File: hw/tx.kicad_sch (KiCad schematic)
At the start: 40 parts, among them T301 BN-43-202_DualPri_CTSec, U301 ICE40UP5K-SG48ITR, Y301 40MHz

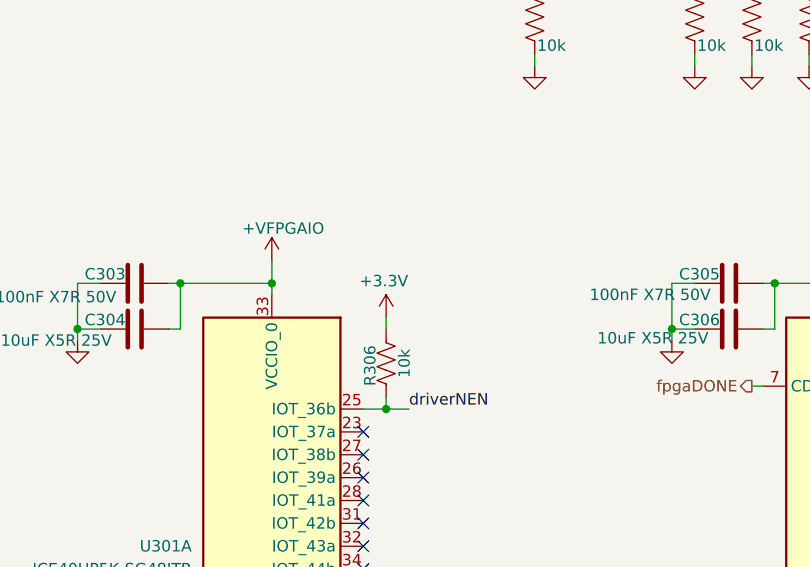
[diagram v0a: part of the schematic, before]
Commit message: Use VFPGAIO for pullup for driverNEN. Fix some layout issues with more equal routing lengths in critical tx phase paths.
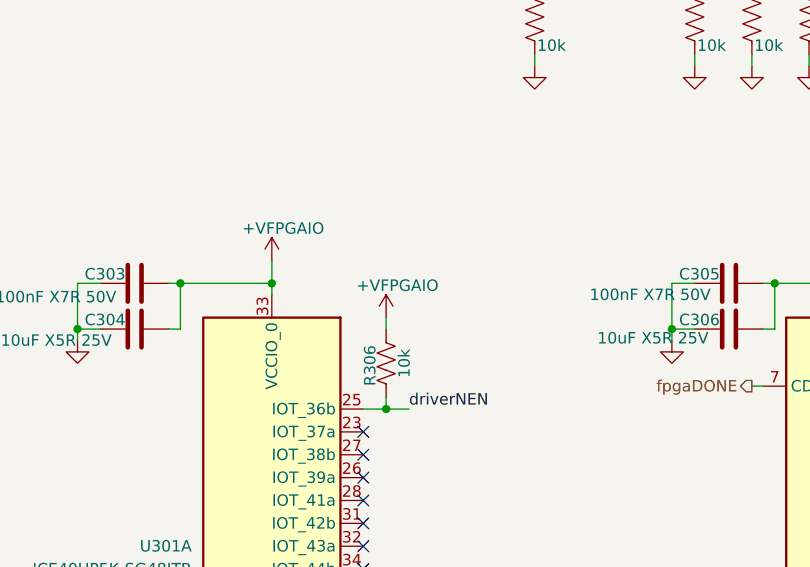
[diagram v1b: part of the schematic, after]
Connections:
- net +3.3V: no longer R306.2
- net +VFPGAIO: now also R306.2
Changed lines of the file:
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@@
-	)
-	(symbol
-		(lib_id "power:+3.3V")
-		(at 66.04 139.7 0)
-		(unit 1)
-		(exclude_from_sim no)
-		(in_bom yes)
-		(on_board yes)
-		(dnp no)
-		(property "Reference" "#PWR0305"
-			(at 66.04 143.51 0)
-			(effects
-				(font
-					(size 1.27 1.27)
-				)
-				(hide yes)
-			)
-		)
-		(property "Value" "+3.3V"
-			(at 65.786 135.636 0)
-			(effects
-				(font
-					(size 1.27 1.27)
-				)
-			)
-		)
-		(property "Footprint" ""
-			(at 66.04 139.7 0)
-			(effects
-				(font
-					(size 1.27 1.27)
-				)
-				(hide yes)
-			)
-		)
-		(property "Datasheet" ""
-			(at 66.04 139.7 0)
-			(effects
-				(font
-					(size 1.27 1.27)
-				)
-				(hide yes)
-			)
-		)
-		(property "Description" "Power symbol creates a global label with name \"+3.3V\""
-			(at 66.04 139.7 0)
-			(effects
-				(font
-					(size 1.27 1.27)
-				)
-				(hide yes)
-			)
-		)
-		(pin "1"
-		)
-		(instances
-			(project "WSPR-ease"
-				(path "/31075357-d7d2-474d-bd47-511c83e129b3/23b3e7ef-2325-4c00-b23e-f86801b0fb79"
-					(reference "#PWR0305")
-					(unit 1)
-				)
-			)
-		)
 	)
 	(symbol
@@
 					(unit 1)
 				)
+			)
+		)
+	)
+	(symbol
+		(lib_id "power:+3.3V")
+		(at 66.04 139.7 0)
+		(unit 1)
+		(exclude_from_sim no)
+		(in_bom yes)
+		(on_board yes)
+		(dnp no)
+		(property "Reference" "#PWR0305"
+			(at 66.04 143.51 0)
+			(effects
+				(font
+					(size 1.27 1.27)
+				)
+				(hide yes)
+			)
+		)
+		(property "Value" "+VFPGAIO"
+			(at 62.738 136.144 0)
+			(effects
+				(font
+					(size 1.27 1.27)
+				)
+				(justify left)
+			)
+		)
+		(property "Footprint" ""
+			(at 66.04 139.7 0)
+			(effects
+				(font
+					(size 1.27 1.27)
+				)
+				(hide yes)
+			)
+		)
+		(property "Datasheet" ""
+			(at 66.04 139.7 0)
+			(effects
+				(font
+					(size 1.27 1.27)
+				)
+				(hide yes)
+			)
+		)
+		(property "Description" "Power symbol creates a global label with name \"+VFPGAIO\""
+			(at 66.04 139.7 0)
+			(effects
+				(font
+					(size 1.27 1.27)
+				)
+				(hide yes)
+			)
+		)
+		(pin "1"
+		)
+		(instances
+			(project "WSPR-ease"
+				(path "/31075357-d7d2-474d-bd47-511c83e129b3/23b3e7ef-2325-4c00-b23e-f86801b0fb79"
+					(reference "#PWR0305")
+					(unit 1)
+				)

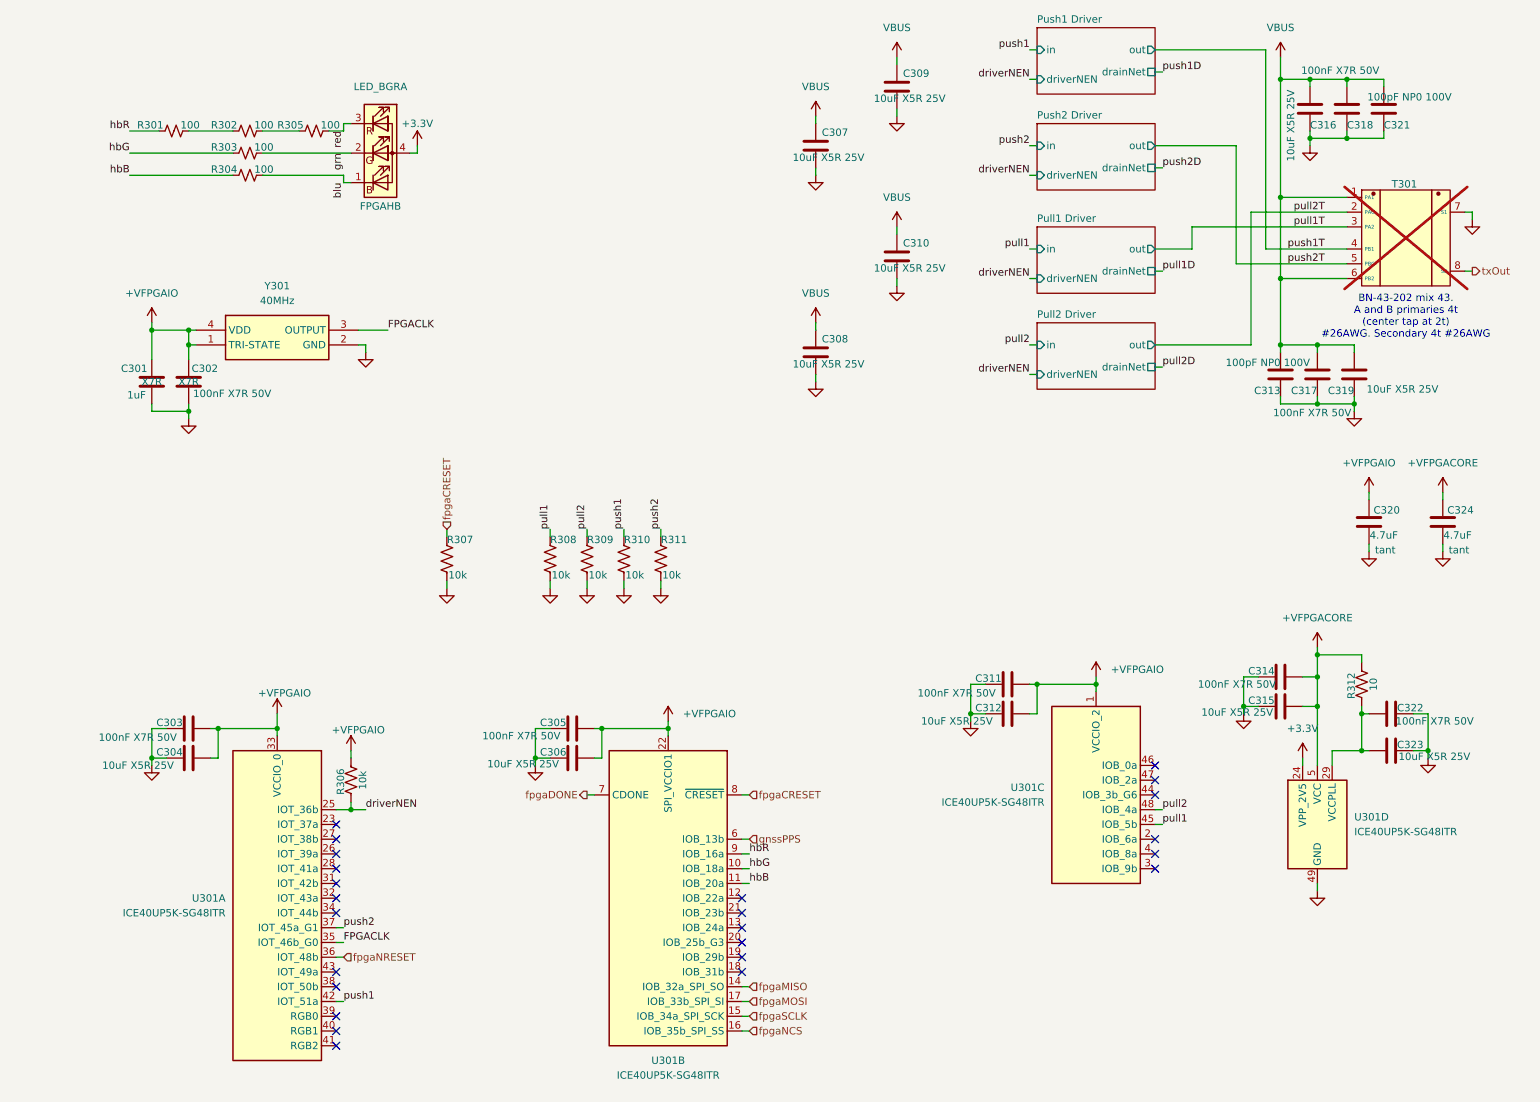
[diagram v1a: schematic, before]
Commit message: I think this is now using the SB_MAC16 properly for each instance. The AI based configs were all screwed up. I listed teh name from the iCE40 Tech Lib doc for each flavor used in a comment to help if changes are needed later. Also silkscreen labels for the four FPGA output pins for probing. I also fixed some stuff in the SB_IO sim cells_sim.v that seemed wrong but now it matches the PDF block diagram AFACT.
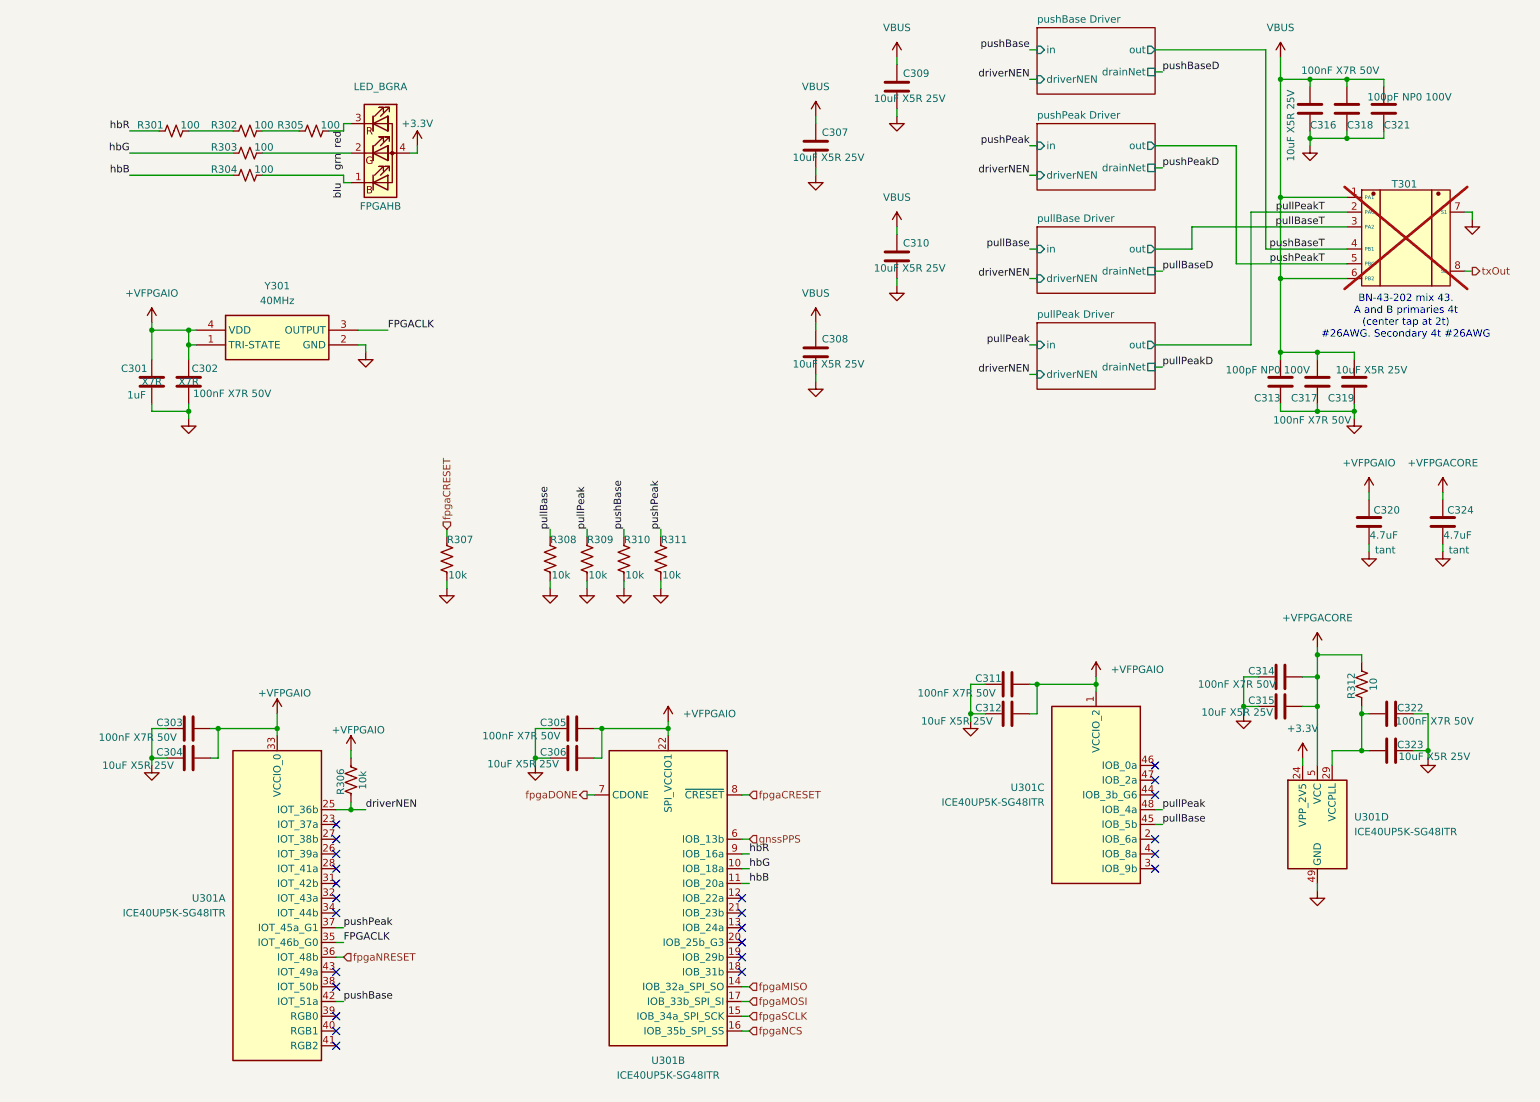
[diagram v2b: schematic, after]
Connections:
- net pull1 renamed pullBase
- net pull1T renamed pullBaseT
- net pull2 renamed pullPeak
- net pull2T renamed pullPeakT
- net push1 renamed pushBase
- net push1T renamed pushBaseT
- net push2 renamed pushPeak
- net push2T renamed pushPeakT
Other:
- sheet Pull1 Driver renamed pullBase Driver
- sheet Pull2 Driver renamed pullPeak Driver
- sheet Push1 Driver renamed pushBase Driver
- sheet Push2 Driver renamed pushPeak Driver
- moved on the sheet: C313, C317, C319

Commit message: Fucking USB 16-pin footprint! Also, completely redid the layout and wiring of the transmitter using a MOSFET gate and R+diode gate drive, simplify BOM, enhance LPFs for square wave output >= 10MHz.
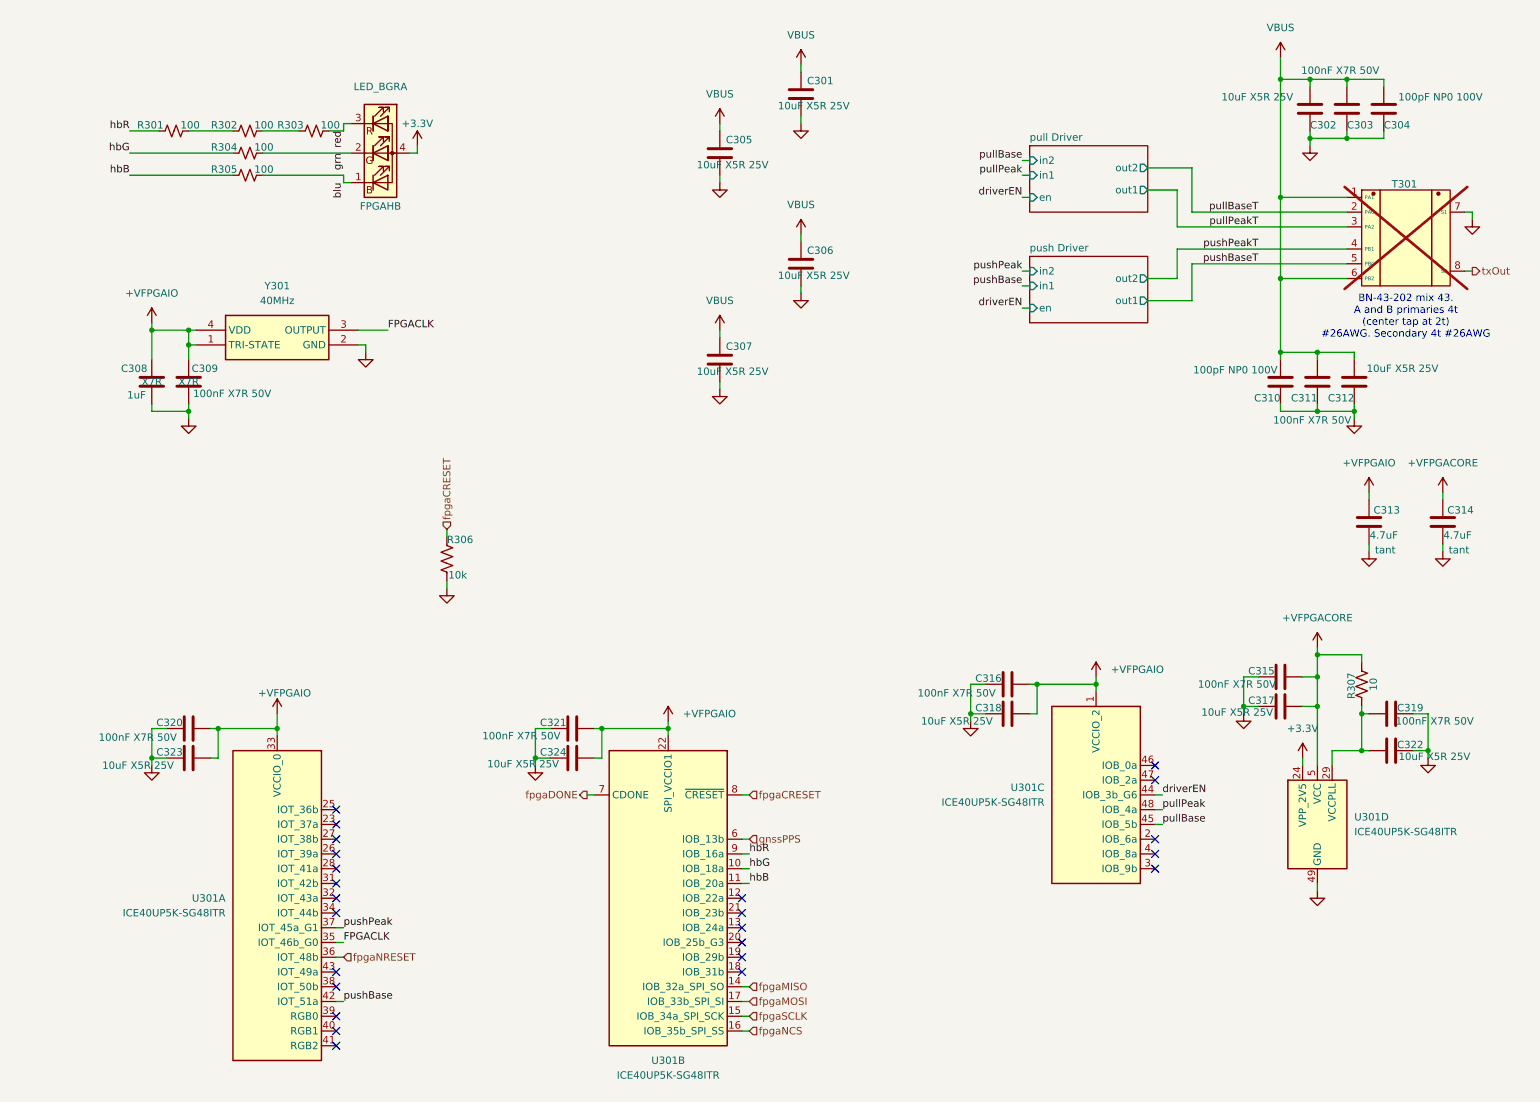
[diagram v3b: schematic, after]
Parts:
- removed R306, R308, R309, R310, R311: 10k, Resistor_SMD:R_0402_1005Metric, symbol Device:R_US
- C301: renamed from C309; working-voltage (none) -> 25V
- C302: renamed from C316; working-voltage (none) -> 25V
- C303: renamed from C318; cap-type (none) -> X7R; working-voltage (none) -> 50V
- C305: renamed from C307; working-voltage (none) -> 25V
- C306: renamed from C310; working-voltage (none) -> 25V
- C307: renamed from C308; working-voltage (none) -> 25V
- C311: renamed from C317; cap-type (none) -> X7R; working-voltage (none) -> 50V
- C312: renamed from C319; working-voltage (none) -> 25V
- C315: renamed from C314; cap-type (none) -> X7R; working-voltage (none) -> 50V
- C316: renamed from C311; cap-type (none) -> X7R; working-voltage (none) -> 50V
- C317: renamed from C315; working-voltage (none) -> 25V
- C318: renamed from C312; working-voltage (none) -> 25V
- C319: renamed from C322; cap-type (none) -> X7R; working-voltage (none) -> 50V
- C320: renamed from C303; cap-type (none) -> X7R; working-voltage (none) -> 50V
- C321: renamed from C305; cap-type (none) -> X7R; working-voltage (none) -> 50V
- C322: renamed from C323; working-voltage (none) -> 25V
- C323: renamed from C304; working-voltage (none) -> 25V
- C324: renamed from C306; working-voltage (none) -> 25V
- R301, R302: MFG (none) -> Bourns; MPN (none) -> CR0402-JW-101GLF; Mouser_PN (none) -> 652-CR0402JW-101GLF
- R303: renamed from R305; MFG (none) -> Bourns; MPN (none) -> CR0402-JW-101GLF; Mouser_PN (none) -> 652-CR0402JW-101GLF
- R304: renamed from R303; MFG (none) -> Bourns; MPN (none) -> CR0402-JW-101GLF; Mouser_PN (none) -> 652-CR0402JW-101GLF
- R305: renamed from R304; MFG (none) -> Bourns; MPN (none) -> CR0402-JW-101GLF; Mouser_PN (none) -> 652-CR0402JW-101GLF
- R306: renamed from R307; MFG Vishay -> Bourns; MPN MCS04020C1002FE000 -> CRT0402-FZ-1003GLF; Mouser_PN 594-MCS04020C1002FE0 -> 652-CRT0402FZ1003GLF
- renumbered C321 to C304, C301 to C308, C302 to C309, C313 to C310, C320 to C313, C324 to C314, R312 to R307
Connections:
- net pullBaseT: now also T301.2 (PAC); no longer T301.3 (PA2)
- net pullPeakT: now also T301.3 (PA2); no longer T301.2 (PAC)
- net pushBaseT: now also T301.5 (PBC); no longer T301.4 (PB1)
- net pushPeakT: now also T301.4 (PB1); no longer T301.5 (PBC)
- net driverEN: now reaches U301.44 (IOB_3b_G6)
- net driverNEN: no longer names the net of U301.25 (IOT_36b)
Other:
- sheet pushBase Driver renamed push Driver
- removed sheet pullBase Driver
- removed sheet pullPeak Driver
- removed sheet pushPeak Driver
- added sheet pull Driver (phase-driver.kicad_sch)
- sheet push Driver ports: added en, in1, in2, out1, out2; removed drainNet, driverNEN, in, out
- moved on the sheet: C301, C305, C306, C307
